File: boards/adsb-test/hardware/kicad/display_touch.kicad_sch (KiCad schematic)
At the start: 0 parts

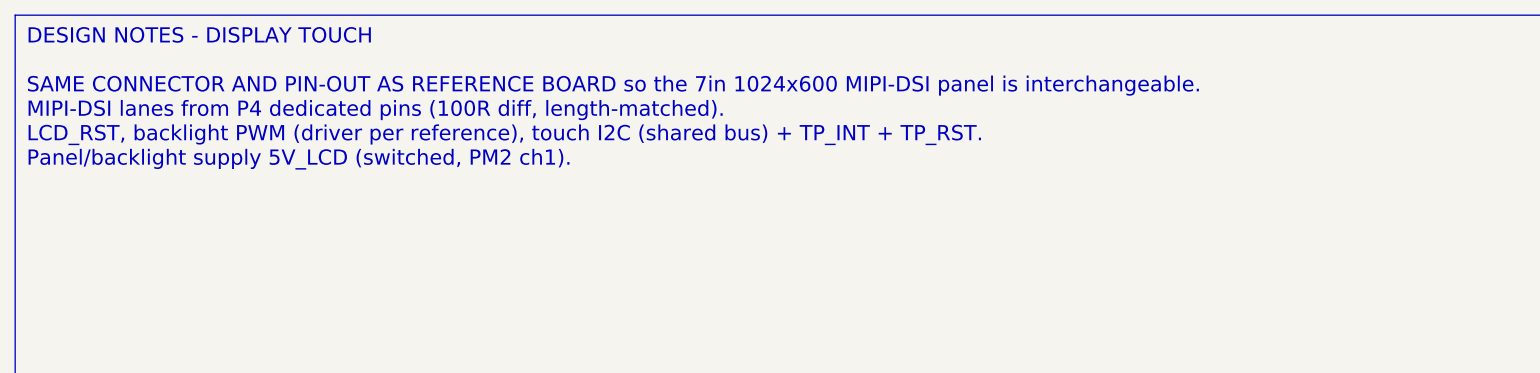
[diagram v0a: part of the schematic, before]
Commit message: Release v0.4.0: ADSB_Test with ESP32-C5, ADSBee m1421 and LA5016 header
- C6 -> C5 co-processor; m1421 identified and integrated (symbol/footprint
  from the ADSBee 1421 carrier, GPL-3.0 attribution)
- Power budget and 2S1P battery sizing for >= 1 h; USB-A for 1-2 SDRs via hub
- Dev port: FT2232H + RP2040 debugprobe; TCA6408A expander for slow I/O
- Test Debug sheet with LA5016 header and rail test points
- Vendor documents git-ignored (public repo)

Co-Authored-By: Claude Opus 5.5 <noreply@anthropic.com>
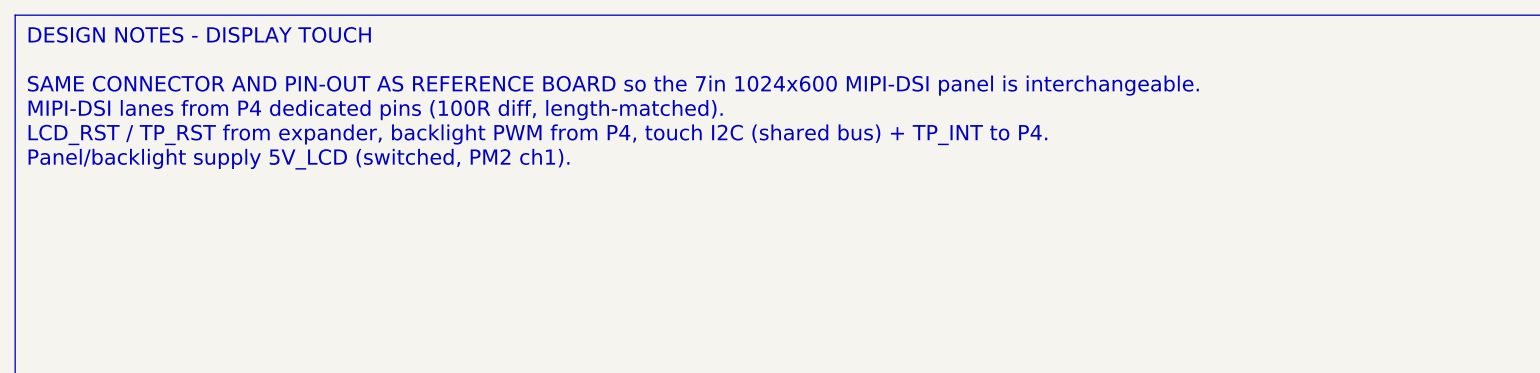
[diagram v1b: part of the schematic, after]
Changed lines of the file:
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@@
 		(comment 1 "Requirements: boards/adsb-test/docs/requirements.md")
 	)
-	(text_box "DESIGN NOTES - DISPLAY TOUCH\n\nSAME CONNECTOR AND PIN-OUT AS REFERENCE BOARD so the 7in 1024x600 MIPI-DSI panel is interchangeable.\nMIPI-DSI lanes from P4 dedicated pins (100R diff, length-matched).\nLCD_RST, backlight PWM (driver per reference), touch I2C (shared bus) + TP_INT + TP_RST.\nPanel/backlight supply 5V_LCD (switched, PM2 ch1)."
+	(text_box "DESIGN NOTES - DISPLAY TOUCH\n\nSAME CONNECTOR AND PIN-OUT AS REFERENCE BOARD so the 7in 1024x600 MIPI-DSI panel is interchangeable.\nMIPI-DSI lanes from P4 dedicated pins (100R diff, length-matched).\nLCD_RST / TP_RST from expander, backlight PWM from P4, touch I2C (shared bus) + TP_INT to P4.\nPanel/backlight supply 5V_LCD (switched, PM2 ch1)."
 		(exclude_from_sim no)
 		(at 20 20 0)
